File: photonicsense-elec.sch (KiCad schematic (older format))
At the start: 0 parts

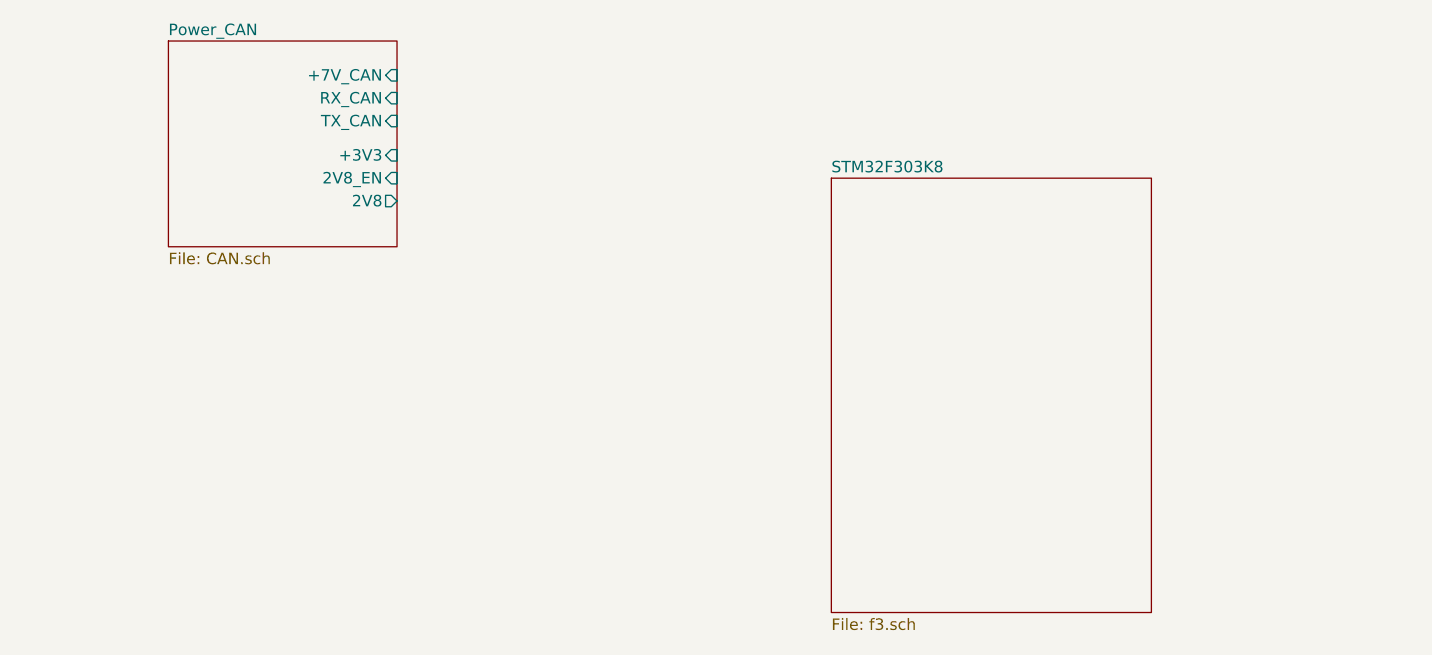
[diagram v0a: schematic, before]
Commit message: Added I2C level shifter
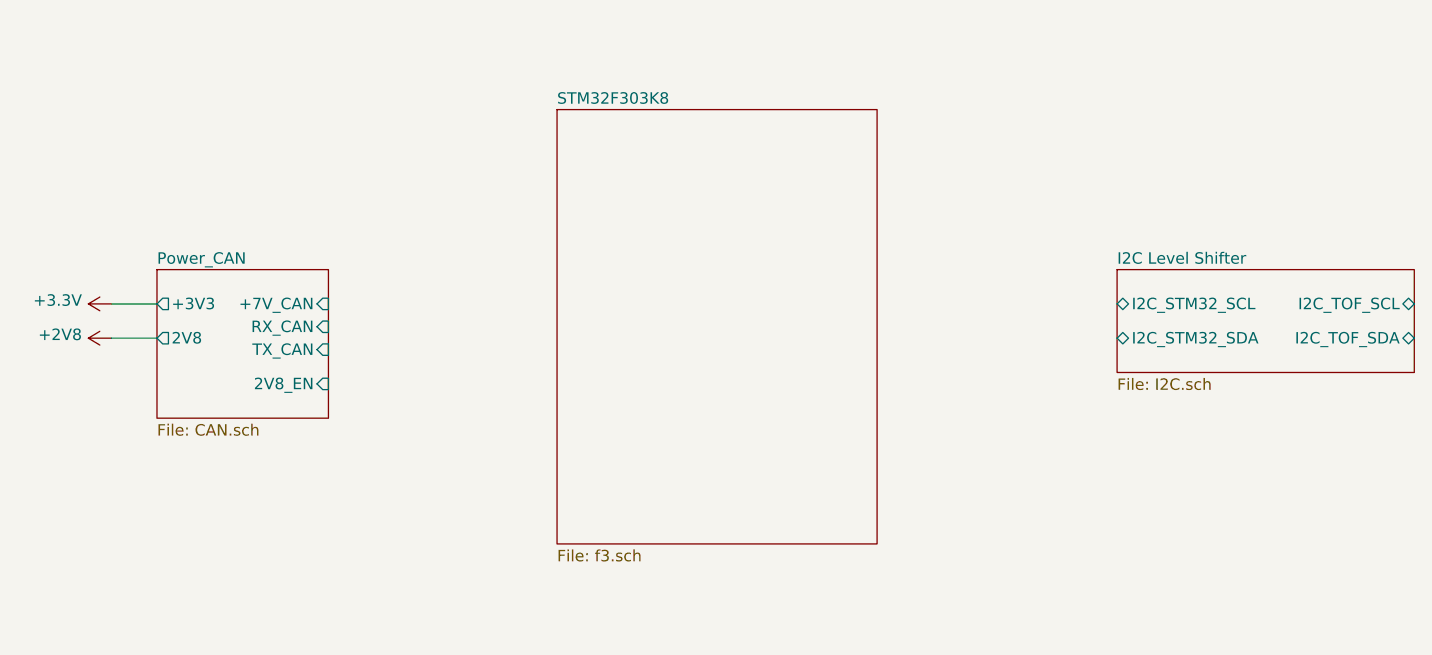
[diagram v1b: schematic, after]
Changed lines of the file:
@@
 $Descr A4 11693 8268
 encoding utf-8
-Sheet 1 3
+Sheet 1 4
 Title ""
 Date ""
@@
 $EndDescr
 $Sheet
-S 1850 1900 1000 900
+S 1800 2900 750  650
 U 5BBA64E1
 F0 "Power_CAN" 50
 F1 "CAN.sch" 50
-F2 "RX_CAN" I R 2850 2150 50
-F3 "TX_CAN" I R 2850 2250 50
-F4 "+7V_CAN" I R 2850 2050 50
-F5 "+3V3" I R 2850 2400 50
-F6 "2V8_EN" I R 2850 2500 50
-F7 "2V8" O R 2850 2600 50
+F2 "RX_CAN" I R 2550 3150 50
+F3 "TX_CAN" I R 2550 3250 50
+F4 "+7V_CAN" I R 2550 3050 50
+F5 "2V8_EN" I R 2550 3400 50
+F6 "2V8" O L 1800 3200 50
+F7 "+3V3" O L 1800 3050 50
 $EndSheet
 $Sheet
-S 4750 2500 1400 1900
+S 3550 2200 1400 1900
 U 5BBD3D7F
 F0 "STM32F303K8" 50
 F1 "f3.sch" 50
 $EndSheet
+$Sheet
+S 6000 2900 1300 450
+U 5BBBF4E0
+F0 "I2C Level Shifter" 50
+F1 "I2C.sch" 50
+F2 "I2C_STM32_SCL" B L 6000 3050 50
+F3 "I2C_STM32_SDA" B L 6000 3200 50
+F4 "I2C_TOF_SCL" B R 7300 3050 50
+F5 "I2C_TOF_SDA" B R 7300 3200 50
+$EndSheet
+$Comp
+L power:+3.3V #PWR?
+U 1 1 5BBBF8DE
+P 1600 3050
+F 0 "#PWR?" H 1600 2900 50  0001 C CNN
+F 1 "+3.3V" V 1615 3178 50  0000 L CNN
+F 2 "" H 1600 3050 50  0001 C CNN
+F 3 "" H 1600 3050 50  0001 C CNN
+	1    1600 3050
+	0    -1   -1   0
+$EndComp
+$Comp
+L power:+2V8 #PWR?
+U 1 1 5BBBF9EE
+P 1600 3200
+F 0 "#PWR?" H 1600 3050 50  0001 C CNN
+F 1 "+2V8" V 1615 3328 50  0000 L CNN
+F 2 "" H 1600 3200 50  0001 C CNN
+F 3 "" H 1600 3200 50  0001 C CNN
+	1    1600 3200
+	0    -1   -1   0
+$EndComp
+Wire Wire Line
+	1600 3050 1800 3050
+Wire Wire Line
+	1600 3200 1800 3200
 $EndSCHEMATC

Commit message: Added ToF connectors and fixed schematic ERC
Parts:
- added J1: Conn_SWD_UART, symbol Connector_Generic:Conn_01x08
- added J2, J3, J4, J5, J6, J7, J8, J9: Conn_01x05, symbol Connector_Generic:Conn_01x05
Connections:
- net labels added: +3V3, +5V, GND, ToF_SCL, ToF_SDA
- wire segments 2 -> 78
- no-connect marks 0 -> 1

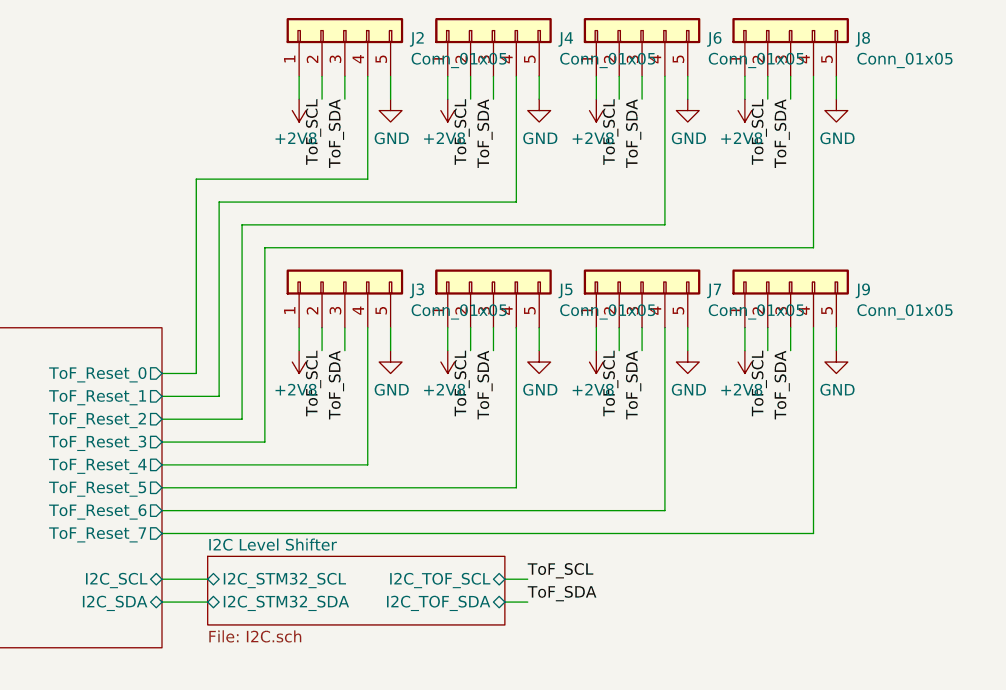
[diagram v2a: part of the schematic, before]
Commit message: Fixed ToF Reset levels
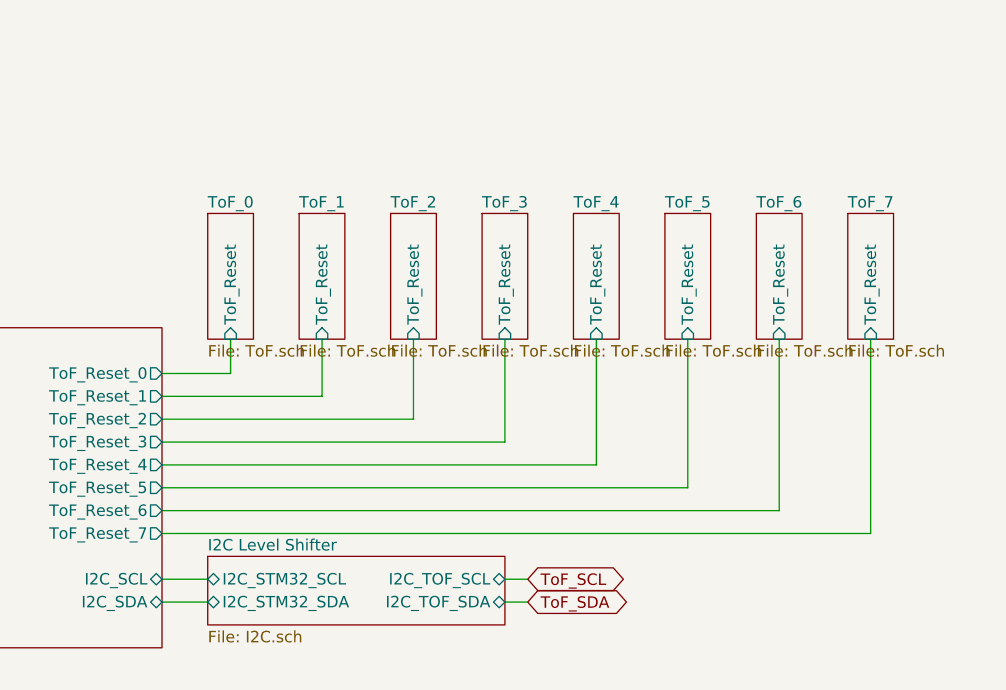
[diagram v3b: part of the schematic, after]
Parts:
- removed J2, J3, J4, J5, J6, J7, J8, J9: Conn_01x05, symbol Connector_Generic:Conn_01x05
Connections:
- wire segments 78 -> 38

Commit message: Added ultrasonic sensors
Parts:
- added Q1: BSS138, Package_TO_SOT_SMD:SOT-23, symbol Transistor_FET:BSS138
- added R1, R2: R, symbol Device:R
- added U1: 74HC164, symbol PhoenixRobotik:74HC164
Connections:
- wire segments 38 -> 67

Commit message: Added power selector for ultrasonic sensors
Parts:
- added JP2: Jumper_NC_Dual, symbol Device:Jumper_NC_Dual
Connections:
- net labels added: US_POWER
- wire segments 67 -> 70
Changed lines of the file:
@@
 Wire Wire Line
 	4850 4200 5700 4200
+$Comp
+L Device:Jumper_NC_Dual JP2
+U 1 1 5BC13B05
+P 1650 3300
+F 0 "JP2" H 1650 3539 50  0000 C CNN
+F 1 "Jumper_NC_Dual" H 1650 3448 50  0000 C CNN
+F 2 "" H 1650 3300 50  0001 C CNN
+F 3 "~" H 1650 3300 50  0001 C CNN
+	1    1650 3300
+	0    -1   -1   0
+$EndComp
+$Comp
+L power:+3.3V #PWR047
+U 1 1 5BC13D95
+P 1650 3650
+F 0 "#PWR047" H 1650 3500 50  0001 C CNN
+F 1 "+3.3V" V 1665 3778 50  0000 L CNN
+F 2 "" H 1650 3650 50  0001 C CNN
+F 3 "" H 1650 3650 50  0001 C CNN
+	1    1650 3650
+	-1   0    0    1
+$EndComp
+$Comp
+L power:+5V #PWR043
+U 1 1 5BC13E1A
+P 1650 2950
+F 0 "#PWR043" H 1650 2800 50  0001 C CNN
+F 1 "+5V" V 1665 3078 50  0000 L CNN
+F 2 "" H 1650 2950 50  0001 C CNN
+F 3 "" H 1650 2950 50  0001 C CNN
+	1    1650 2950
+	1    0    0    -1
+$EndComp
+Text GLabel 1850 3300 2    50   Output ~ 0
+US_POWER
+Wire Wire Line
+	1650 3650 1650 3550
+Wire Wire Line
+	1750 3300 1850 3300
+Wire Wire Line
+	1650 3050 1650 2950
 $EndSCHEMATC
